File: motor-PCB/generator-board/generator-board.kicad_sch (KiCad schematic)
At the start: 31 parts, among them J1 Conn_02x05_Odd_Even, J2 Conn_01x02, Q1 PMOS, Q10 NMOS, Q6 NMOS, Q7 NMOS, Q8 NMOS, Q9 NMOS, U2 TMP117xxDRV, U3 INA219BxDCN

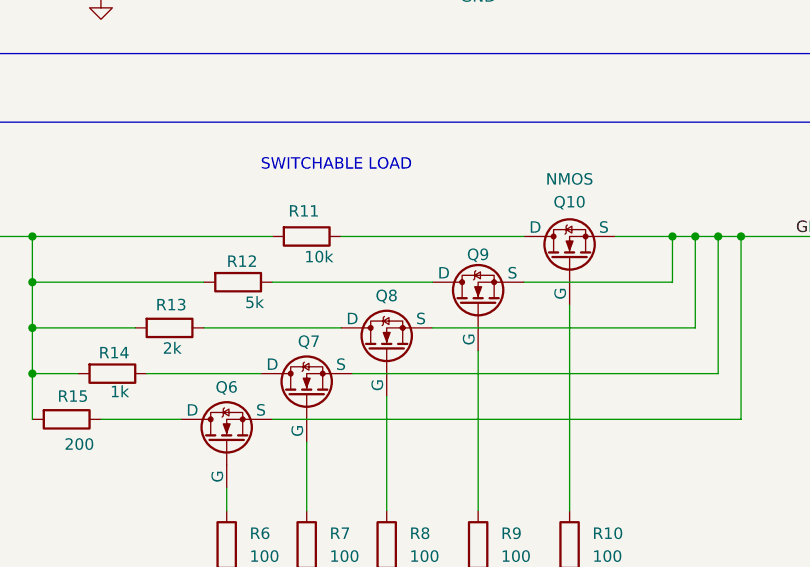
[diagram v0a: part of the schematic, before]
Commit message: added a missing capacitor in the control-board. Added pins to be able to control the heating pad and fan and text. In the generator changed the transistor layout and also added text
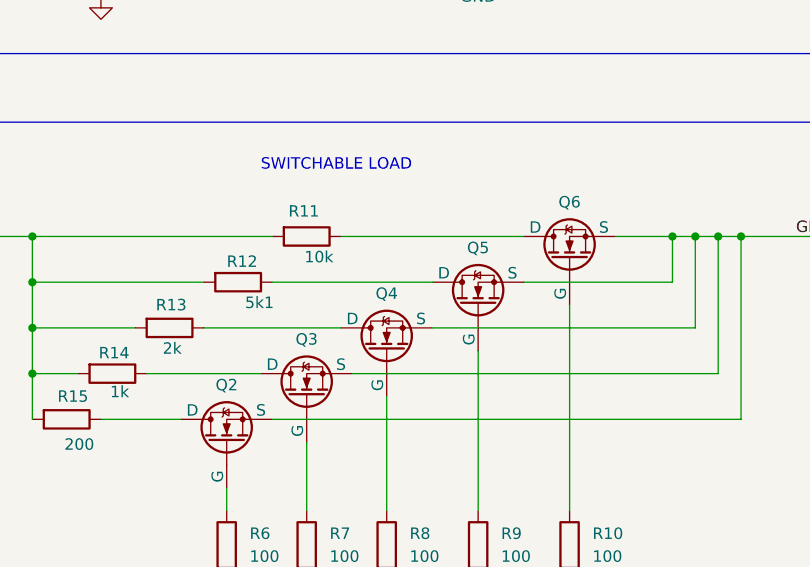
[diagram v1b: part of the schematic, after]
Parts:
- removed Q10, Q6, Q7, Q8, Q9: NMOS, Package_TO_SOT_THT:TO-220-3_Vertical, symbol Simulation_SPICE:NMOS
- added Q2, Q3, Q4, Q5, Q6: NMOS_GDS, Package_TO_SOT_THT:TO-220-3_Vertical, symbol Custom:NMOS_GDS
- R1, R10, R11, R13, R14, R15, R16, R17, R18, R19, R20, R6, R7, R8, R9: footprint Resistor_THT:R_Axial_DIN0207_L6.3mm_D2.5mm_P7.62mm_Horizontal -> Resistor_THT:R_Axial_DIN0207_L6.3mm_D2.5mm_P10.16mm_Horizontal
- R12: value 5k -> 5k1; footprint Resistor_THT:R_Axial_DIN0207_L6.3mm_D2.5mm_P7.62mm_Horizontal -> Resistor_THT:R_Axial_DIN0207_L6.3mm_D2.5mm_P10.16mm_Horizontal
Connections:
- net GND: now also Q2.3 (S), Q3.3 (S), Q4.3 (S), Q5.3 (S), Q6.3 (S)
- net at R11.1: now also Q6.2 (D)
- net at R14.1: now also Q3.2 (D)
- net at R7.1: now also Q3.1 (G)
- net at R12.1: now also Q5.2 (D)
- net at R9.1: now also Q5.1 (G)
- net at R6.1: now also Q2.1 (G)
- net at R13.1: now also Q4.2 (D)
- net at R15.1: now also Q2.2 (D)
- net at R10.1: now also Q6.1 (G)
- net at R8.1: now also Q4.1 (G)

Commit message: forgot to change the layout of the pmos so fixed that
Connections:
- net GENERATOR_IN: now also Q1.2 (D); no longer Q1.1 (D)
- net at R1.1: now also Q1.1 (G); no longer Q1.2 (G)
